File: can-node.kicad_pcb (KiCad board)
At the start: 2 copper layers, 43 parts, among them J1 Conn_01x02_Pin, J10 Conn_01x06_Pin, J11 Conn_01x01_Socket, J12 Conn_01x01_Socket, J13 Conn_01x01_Socket, J14 Conn_01x01_Socket, J15 Conn_01x01_Socket, J16 Conn_01x01_Socket, J17 Conn_01x01_Socket, J18 Conn_01x01_Socket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

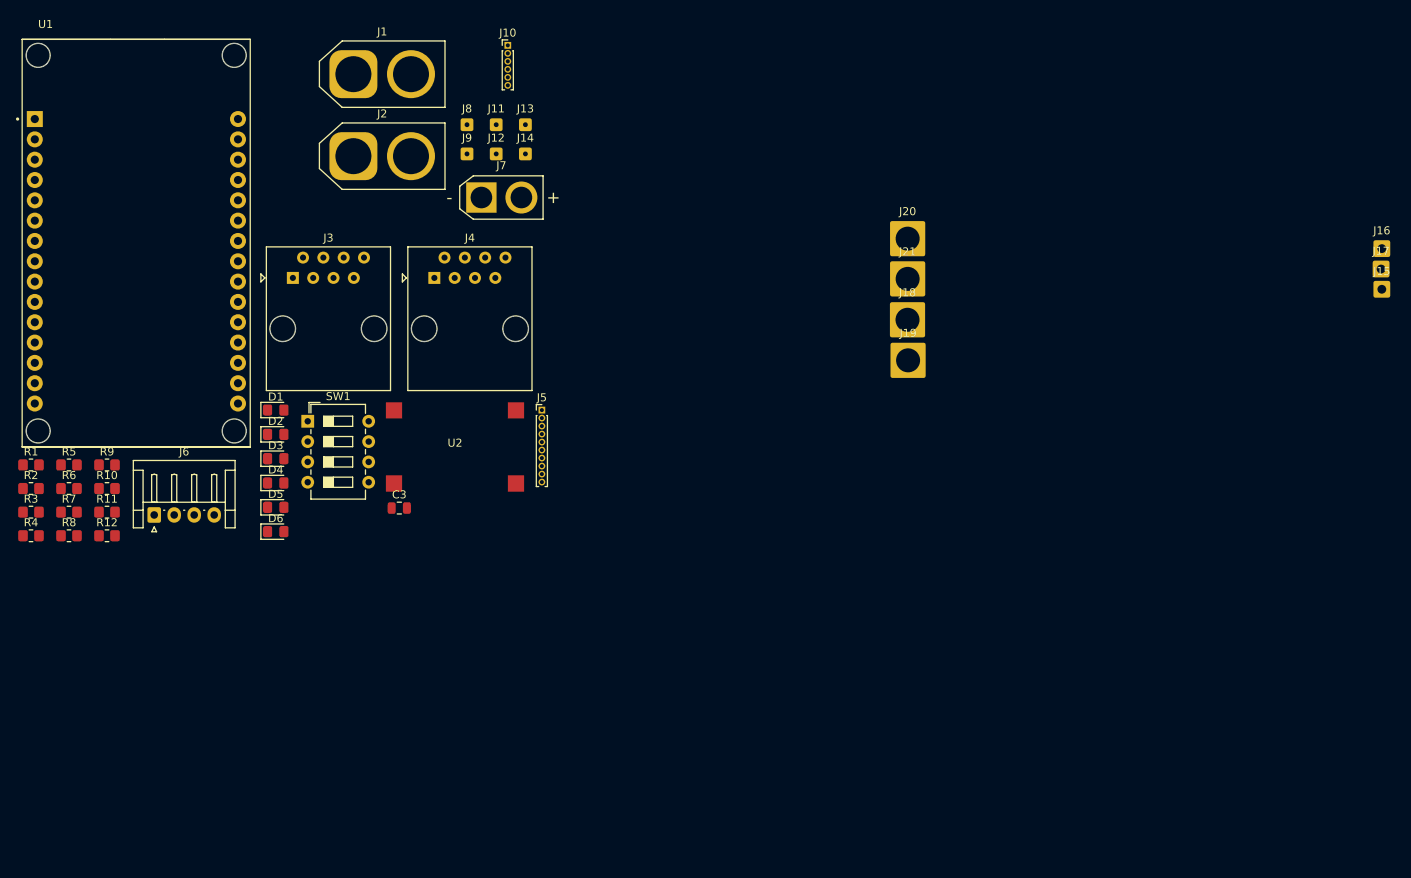
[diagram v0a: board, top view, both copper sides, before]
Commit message: placed PCB components
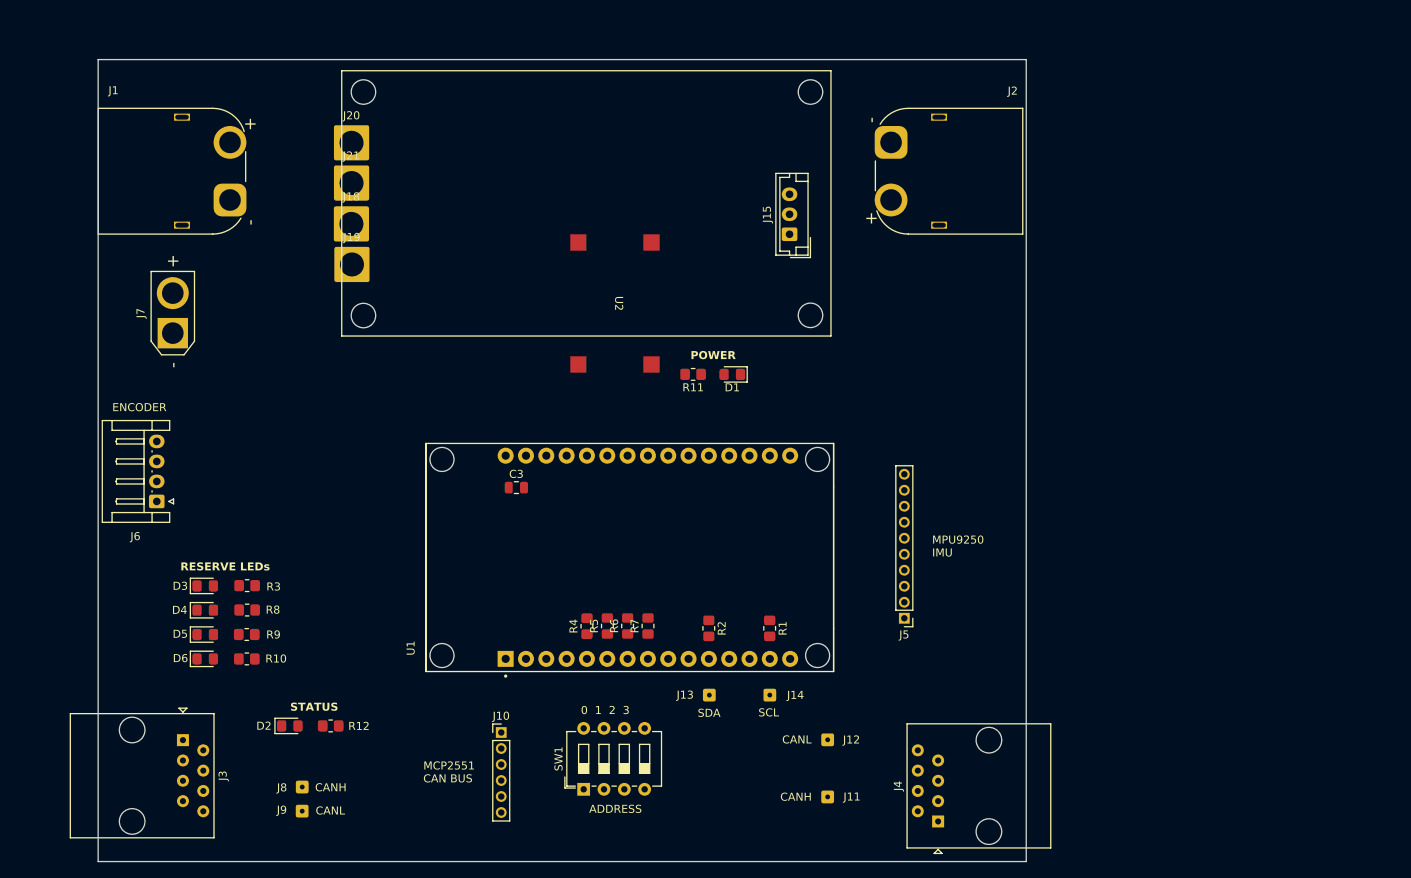
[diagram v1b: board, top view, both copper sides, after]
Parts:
- removed J16, J17: Conn_01x01_Socket, Connector_Wire:SolderWire-0.5sqmm_1x01_D0.9mm_OD2.1mm
- J1: footprint Connector_AMASS:AMASS_XT60-F_1x02_P7.20mm_Vertical -> Connector_AMASS:AMASS_XT60PW-M_1x02_P7.20mm_Horizontal
- J10: footprint Connector_PinHeader_1.00mm:PinHeader_1x06_P1.00mm_Vertical -> Connector_PinHeader_2.00mm:PinHeader_1x06_P2.00mm_Vertical
- J15: value Conn_01x01_Socket -> Conn_01x03_Pin; footprint Connector_Wire:SolderWire-0.5sqmm_1x01_D0.9mm_OD2.1mm -> Connector_JST:JST_EH_B3B-EH-A_1x03_P2.50mm_Vertical
- J2: footprint Connector_AMASS:AMASS_XT60-M_1x02_P7.20mm_Vertical -> Connector_AMASS:AMASS_XT60PW-M_1x02_P7.20mm_Horizontal
- J5: footprint Connector_PinHeader_1.00mm:PinHeader_1x10_P1.00mm_Vertical -> Connector_PinHeader_2.00mm:PinHeader_1x10_P2.00mm_Vertical
- moved R1 94.6 mm to (114.8, 94.5), turned to -90 degrees
- moved J11 93.7 mm to (122.1, 115.6)
- moved J4 92.6 mm to (135.9, 118.6), turned to 90 degrees
- moved R2 86.5 mm to (107.2, 94.5), turned to -90 degrees
- moved J10 85.9 mm to (81.3, 107.5)
- moved J8 85.3 mm to (56.4, 114.3)
- moved J9 84.7 mm to (56.4, 117.3)
- moved J12 84.1 mm to (122.1, 108.4)
- moved R11 75.3 mm to (105.3, 62.7), turned to 180 degrees
- moved J13 74.9 mm to (107.3, 102.8)
- moved J15 74.4 mm to (117.3, 45.2), turned to 90 degrees
- moved J14 74.2 mm to (114.9, 102.8)
- moved R7 73.8 mm to (99.6, 94.2), turned to 90 degrees
- moved U1 73.1 mm to (97.3, 85.6), turned to 90 degrees
- moved R6 71.9 mm to (97.1, 94.2), turned to 90 degrees
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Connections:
- J13 pad 1: CAN+ -> I2C-SDA
- J14 pad 1: CAN- -> I2C-SCL
- R2 pad 2: I2C-SCL -> I2C-SDA
- U1 pad 10: I2C-SCL -> FSYNC
- U1 pad 14: ADD0 -> I2C-SCL
- U1 pad 15: ADD1 -> unconnected-(U1-D23-Pad15)
- U1 pad 20: ENC-A -> unconnected-(U1-D35-Pad20)
- U1 pad 21: DIR -> STATUS
- U1 pad 22: STATUS -> ENC-A
- U1 pad 23: ADD2 -> PWM
- U1 pad 24: ADD3 -> DIR
- U1 pad 25: PWM -> LED3
- U1 pad 26: CAN-Tx -> LED2
- U1 pad 27: LED3 -> LED1
- U1 pad 28: CAN-Rx -> LED0
- U1 pad 3: INT -> CAN-Tx
- U1 pad 4: LED0 -> CAN-Rx
- U1 pad 5: LED1 -> ADD0
- U1 pad 6: unconnected-(U1-RX2-Pad6) -> ADD1
- U1 pad 7: unconnected-(U1-TX2-Pad7) -> ADD2
- U1 pad 8: LED2 -> ADD3
- U1 pad 9: FSYNC -> INT
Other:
- board outline added: 116 x 100.2 mm
- board text added: "0 1 2 3"
- board text added: "ADDRESS"
- board text added: "CANH"
- board text added: "CANL"
- board text added: "ENCODER"
- board text added: "MCP2551 CAN BUS"
- board text added: "MPU9250 IMU"
- board text added: "POWER"
- board text added: "RESERVE LEDs"
- board text added: "SCL"
- board text added: "SDA"
- board text added: "STATUS"

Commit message: additional labelling
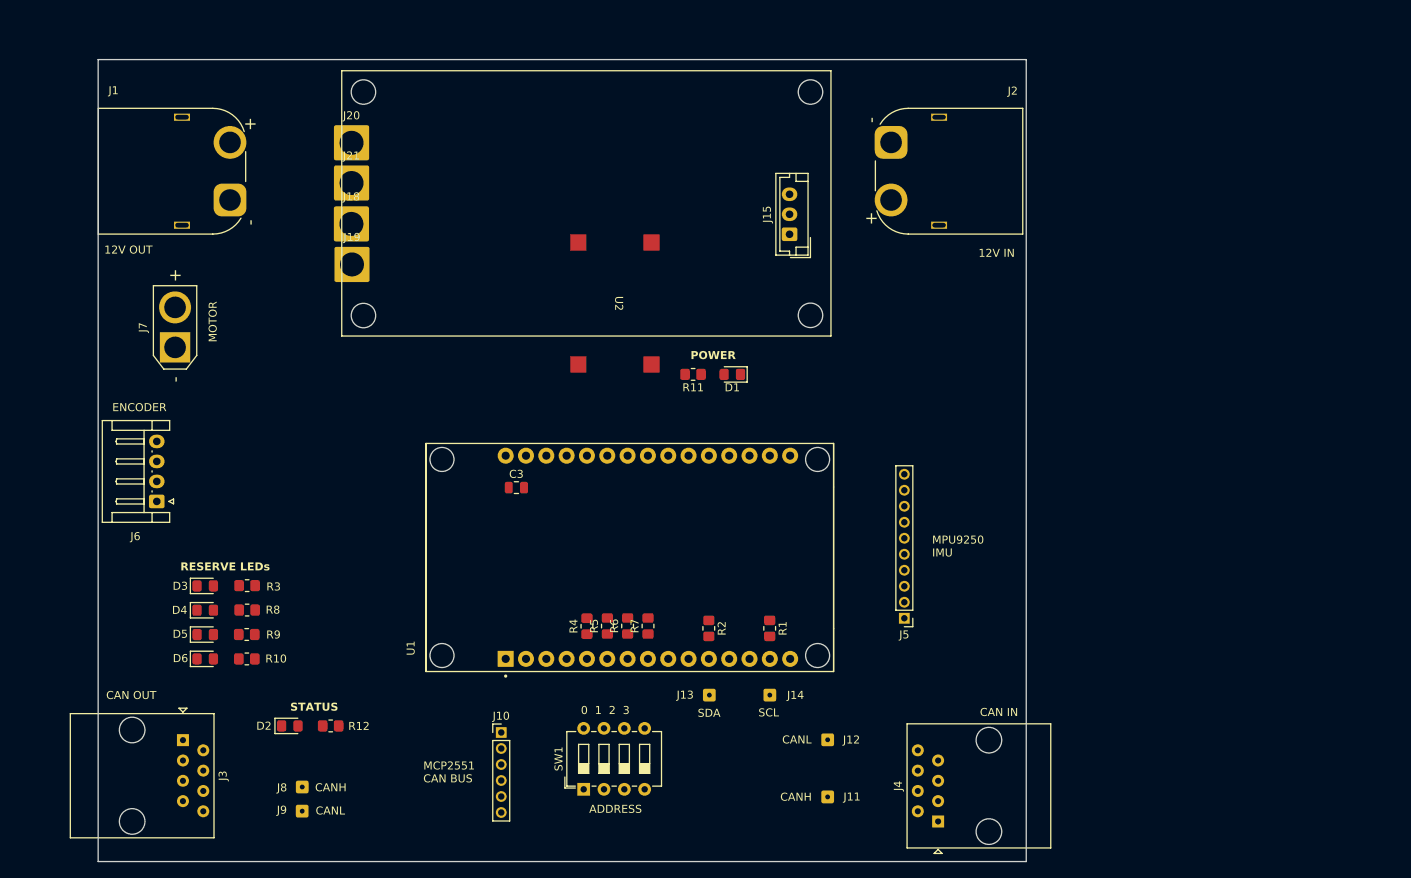
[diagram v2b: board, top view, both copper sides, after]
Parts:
- moved J7 1.81 mm to (40.5, 59.4)
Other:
- board text added: "12V IN"
- board text added: "12V OUT"
- board text added: "CAN IN"
- board text added: "CAN OUT"
- board text added: "MOTOR"
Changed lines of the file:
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@@
   )
   (footprint "Connector_AMASS:AMASS_XT30U-F_1x02_P5.0mm_Vertical" (layer "F.Cu")
-    (at 40.225596 57.580518 90)
+    (at 40.508441 59.364121 90)
     (descr "Connector XT30 Vertical Cable Female, https://www.tme.eu/en/Document/3cbfa5cfa544d79584972dd5234a409e/XT30U%20SPEC.pdf")
     (tags "RC Connector XT30")
@@
     (effects (font (size 1 1) (thickness 0.2) bold) (justify left bottom))
   )
+  (gr_text "CAN OUT" (at 31.892911 103.437603) (layer "F.SilkS")
+    (effects (font (size 1 1) (thickness 0.15)) (justify left bottom))
+  )
+  (gr_text "12V IN" (at 140.933526 48.167815) (layer "F.SilkS")
+    (effects (font (size 1 1) (thickness 0.15)) (justify left bottom))
+  )
   (gr_text "CANL" (at 58.075146 117.874654) (layer "F.SilkS")
     (effects (font (size 1 1) (thickness 0.15)) (justify left bottom))
@@
     (effects (font (size 1 1) (thickness 0.15)) (justify left bottom))
   )
+  (gr_text "CAN IN" (at 141.112147 105.559816) (layer "F.SilkS")
+    (effects (font (size 1 1) (thickness 0.15)) (justify left bottom))
+  )
   (gr_text "CANL" (at 116.394044 108.993521) (layer "F.SilkS")
     (effects (font (size 1 1) (thickness 0.15)) (justify left bottom))
@@
     (effects (font (size 1 1) (thickness 0.15)) (justify left bottom))
   )
+  (gr_text "MOTOR" (at 45.829862 58.73564 90) (layer "F.SilkS")
+    (effects (font (size 1 1) (thickness 0.15)) (justify left bottom))
+  )
+  (gr_text "12V OUT" (at 31.652709 47.759284) (layer "F.SilkS")
+    (effects (font (size 1 1) (thickness 0.15)) (justify left bottom))
+  )

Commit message: draft?
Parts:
- removed J11, J12: Conn_01x01_Socket, Connector_Wire:SolderWire-0.1sqmm_1x01_D0.4mm_OD1mm
- removed J18, J19, J20, J21: Conn_01x01_Socket, Connector_Wire:SolderWire-2.5sqmm_1x01_D2.4mm_OD4.4mm
- added J16: Conn_01x02_Pin, Connector_Wire:SolderWire-1sqmm_1x02_P5.4mm_D1.4mm_OD2.7mm, F.Cu at (64.1, 73.2)
- added J17: Conn_01x02_Pin, Connector_Wire:SolderWire-1sqmm_1x02_P5.4mm_D1.4mm_OD2.7mm, F.Cu at (64.1, 63.0)
- added R13: 60, Resistor_THT:R_Axial_DIN0207_L6.3mm_D2.5mm_P10.16mm_Horizontal, F.Cu at (114.0, 88.9)
- D1, D2, D3, D4, D5, D6: footprint LED_SMD:LED_0805_2012Metric_Pad1.15x1.40mm_HandSolder -> LED_THT:LED_D3.0mm
- J1, J2: footprint Connector_AMASS:AMASS_XT60PW-M_1x02_P7.20mm_Horizontal -> Connector_Wire:SolderWire-1.5sqmm_1x02_P7.8mm_D1.7mm_OD3.9mm
- J7: footprint Connector_AMASS:AMASS_XT30U-F_1x02_P5.0mm_Vertical -> Connector_Wire:SolderWire-1.5sqmm_1x02_P7.8mm_D1.7mm_OD3.9mm
- R1, R10, R11, R12, R2, R3, R4, R5, R6, R7, R8, R9: footprint Resistor_SMD:R_0805_2012Metric_Pad1.20x1.40mm_HandSolder -> Resistor_THT:R_Axial_DIN0207_L6.3mm_D2.5mm_P10.16mm_Horizontal
- moved D2 82.1 mm to (108.5, 44.5)
- moved J9 79.3 mm to (127.5, 82.3)
- moved J8 79.3 mm to (127.5, 79.2)
- moved R12 72.3 mm to (95.5, 43.7)
- moved D4 62.8 mm to (106.3, 102.3), turned to 90 degrees
- moved D3 58.6 mm to (101.4, 102.3), turned to 90 degrees
- moved R8 56.9 mm to (106.3, 96.3), turned to 90 degrees
- moved J14 54.4 mm to (127.8, 50.0), turned to 180 degrees
- moved J13 53.9 mm to (127.8, 53.0)
- moved R3 52.4 mm to (101.4, 96.3), turned to 90 degrees
- moved D6 30.7 mm to (74.7, 102.3), turned to 90 degrees
- moved R1 30.7 mm to (111.0, 64.0)
- moved R2 30.7 mm to (103.4, 64.0)
- moved J3 27.2 mm to (61.2, 89.7)
- moved D5 26.6 mm to (69.9, 102.3), turned to 90 degrees
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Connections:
- J8 pad 1: CAN+ -> CAN-Rx
- J9 pad 1: CAN- -> CAN-Tx
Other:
- board size 116 x 100.2 mm -> 79 x 73.4 mm
- board text added: "78.9 mm X 73.4 mm"
- board text added: "CRX"
- board text added: "CTX"
- board text removed: "CANH"
- board text removed: "CANL"
- board text removed: "MCP2551 CAN BUS"
- board text removed: "MPU9250 IMU"
- board text removed: "RESERVE LEDs"

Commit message: first try
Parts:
- J13: value Conn_01x01_Socket -> SDA
- J14: value Conn_01x01_Socket -> SCL
- J7: footprint Connector_Wire:SolderWire-1.5sqmm_1x02_P7.8mm_D1.7mm_OD3.9mm -> Connector_Wire:SolderWire-1sqmm_1x02_P5.4mm_D1.4mm_OD2.7mm
- J8: value Conn_01x01_Socket -> CRX
- J9: value Conn_01x01_Socket -> CTX
- R1, R10, R11, R12, R13, R2, R3, R4, R5, R6, R7, R8, R9: footprint Resistor_THT:R_Axial_DIN0207_L6.3mm_D2.5mm_P10.16mm_Horizontal -> Resistor_THT:R_Axial_DIN0204_L3.6mm_D1.6mm_P5.08mm_Horizontal
- moved J1 92.1 mm to (147.6, 50.1)
- moved J3 81.7 mm to (142.0, 102.1), turned to 90 degrees
- moved D5 79.7 mm to (141.0, 66.3), turned to 180 degrees
- moved D6 77.8 mm to (141.0, 61.5), turned to 180 degrees
- moved J7 68.2 mm to (111.9, 41.9), turned to 0 degrees
- moved D3 64.5 mm to (141.0, 51.3), turned to 180 degrees
- moved R9 61.3 mm to (125.0, 69.3), turned to 0 degrees
- moved J17 59.9 mm to (121.9, 47.2), turned to 0 degrees
- moved D4 57.6 mm to (141.0, 56.4), turned to 180 degrees
- moved R10 55.8 mm to (125.0, 71.9), turned to 0 degrees
- moved J16 54.3 mm to (111.8, 47.2), turned to 0 degrees
- moved D2 52.8 mm to (141.0, 86.1), turned to 180 degrees
- moved D1 52.6 mm to (141.0, 81.0)
- moved R11 51.6 mm to (138.4, 77.0), turned to 90 degrees
- moved R12 51.4 mm to (129.8, 82.0), turned to 180 degrees
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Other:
- board size 79 x 73.4 mm -> 68.6 x 69.1 mm
- board text added: "68.58 mm X 69.088 mm"
- board text removed: "0 1 2 3"
- board text removed: "12V IN"
- board text removed: "12V OUT"
- board text removed: "78.9 mm X 73.4 mm"
- board text removed: "ADDRESS"
- board text removed: "CAN IN"
- board text removed: "CAN OUT"
- board text removed: "CRX"
- board text removed: "CTX"
- board text removed: "ENCODER"
- board text removed: "MOTOR"
- board text removed: "POWER"
- board text removed: "SCL"
- board text removed: "SDA"
- board text removed: "STATUS"
